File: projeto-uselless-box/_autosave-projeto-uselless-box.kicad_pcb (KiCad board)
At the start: 2 copper layers, 10 parts, among them J2 Conn_Para_Fita, M1 Motor_Servo, M2 Motor_Servo, M3 Motor_Servo, SW1 SW_DPST_x2

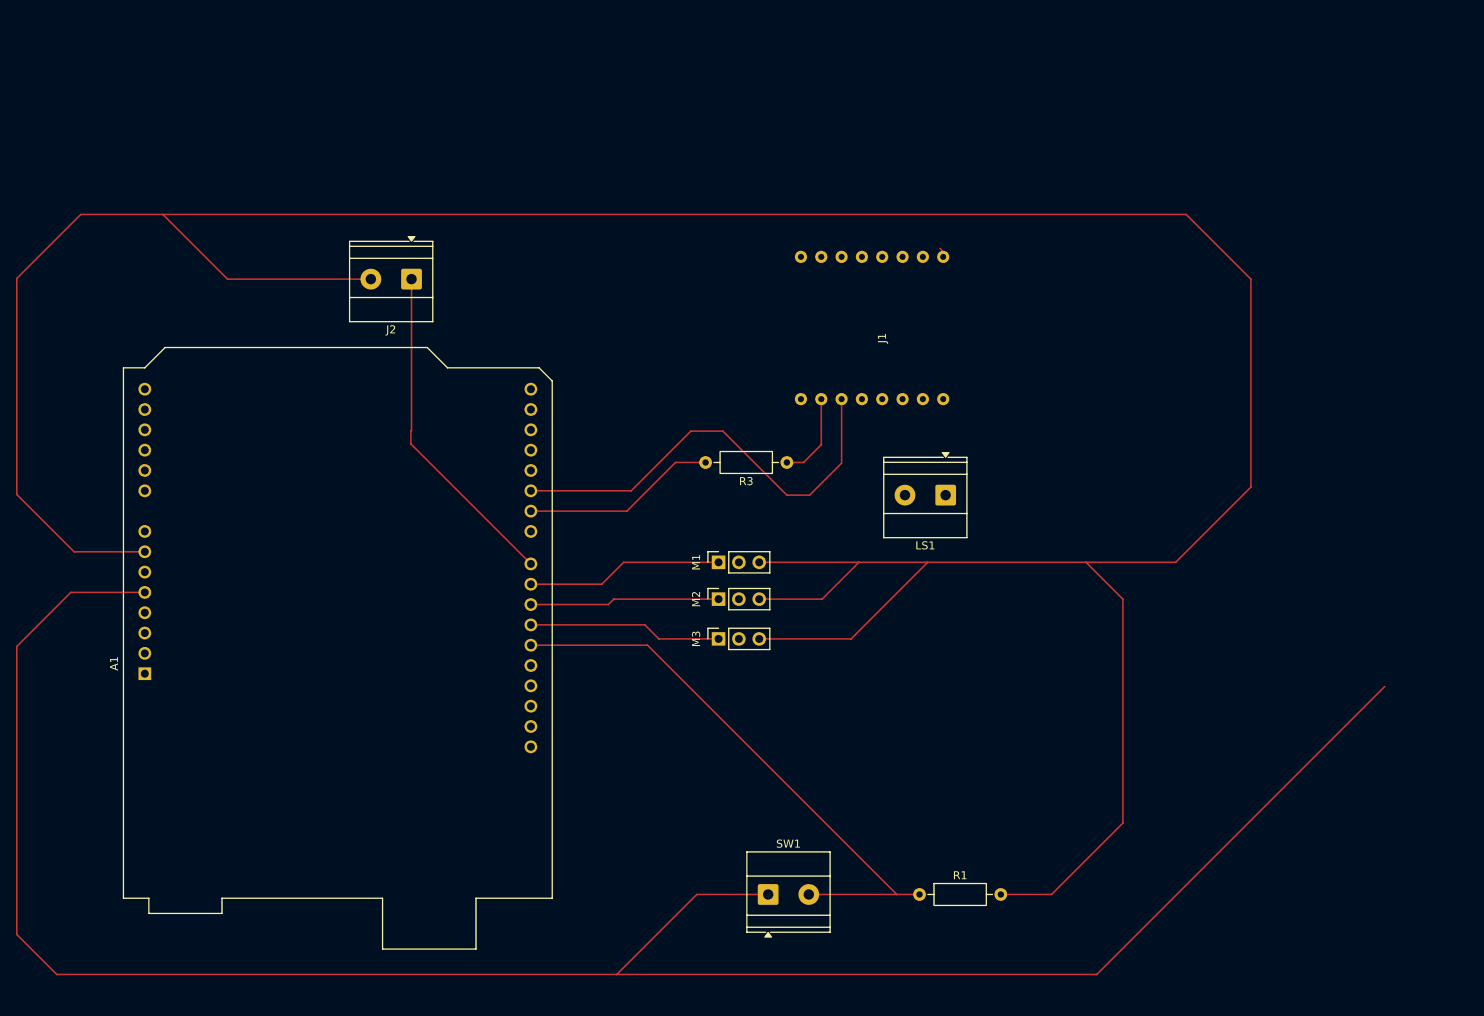
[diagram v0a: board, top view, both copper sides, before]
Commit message: Working in the Transistor of LED strip
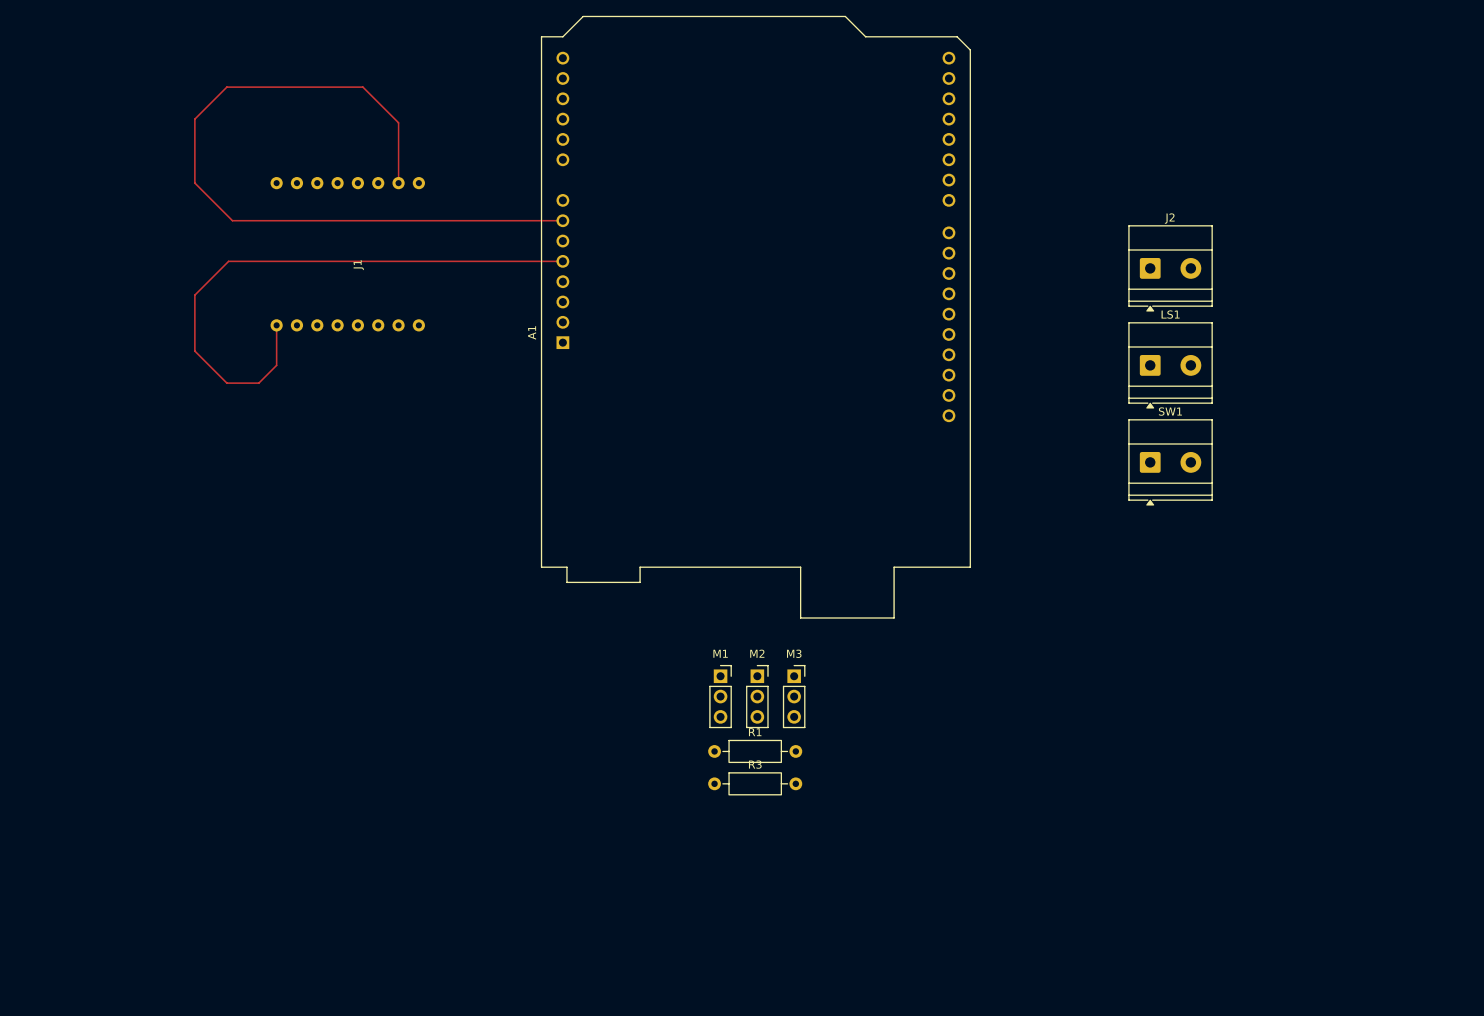
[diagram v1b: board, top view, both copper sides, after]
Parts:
- moved J2 92.3 mm to (184.4, 58.7), turned to 0 degrees
- moved SW1 72.1 mm to (184.4, 82.9)
- moved A1 66.7 mm to (111.0, 67.9)
- moved J1 66.2 mm to (75.2, 58.2)
- moved R3 41.2 mm to (130.0, 123.1), turned to 0 degrees
- moved R1 31.2 mm to (130.0, 119.0)
- moved LS1 30.3 mm to (184.4, 70.8), turned to 0 degrees
- moved M1 14.2 mm to (130.7, 109.6), turned to 0 degrees
- moved M2 10.8 mm to (135.3, 109.6), turned to 0 degrees
- moved M3 10.5 mm to (139.9, 109.6), turned to 0 degrees
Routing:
- net GND: track 420.5 -> 92.5 mm
- net +5V: track 265.8 -> 72.5 mm
- net D12: track 72.5 -> 0.00 mm
- net D5: track 54.9 -> 0.00 mm
- net D8: track 41.8 -> 0.00 mm
- net D9: track 24.6 -> 0.00 mm
- net D6: track 24.4 -> 0.00 mm
- net D11: track 24.2 -> 0.00 mm
- net D10: track 23.7 -> 0.00 mm
- net Net-(J1-RX): track 10.9 -> 0.00 mm

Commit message: Finished the first prototype of PCB
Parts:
- added J3: Conn_Para_PowerBank, TerminalBlock_Phoenix:TerminalBlock_Phoenix_MKDS-1,5-2-5.08_1x02_P5.08mm_Horizontal, F.Cu at (195.8, 73.8)
- added Q1: TIP41, Package_TO_SOT_THT:TO-220-3_Vertical, F.Cu at (181.1, 88.4)
- added R2: 100R, Resistor_THT:R_Axial_DIN0207_L6.3mm_D2.5mm_P10.16mm_Horizontal, F.Cu at (163.2, 88.4)
- M1, M2, M3: value Motor_Servo -> Motor_Servo-Edit; footprint Connector_PinSocket_2.54mm:PinSocket_1x03_P2.54mm_Vertical -> Connector_PinSocket_2.54mm:PinSocket_1x02_P2.54mm_Vertical
- moved LS1 97.4 mm to (96.0, 111.6), turned to 180 degrees
- moved M1 89.1 mm to (215.0, 80.8)
- moved M2 82.2 mm to (215.0, 89.4)
- moved M3 75.8 mm to (215.0, 99.3)
- moved R1 57.4 mm to (187.4, 118.4)
- moved R3 50.6 mm to (81.0, 110.4), turned to -90 degrees
- moved J2 40.4 mm to (195.8, 97.5), turned to -90 degrees
- moved SW1 38.9 mm to (168.5, 118.4)
- moved J1 34.5 mm to (78.2, 92.5)
- moved A1 34.5 mm to (108.7, 102.3)
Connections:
- J2 pad 1: D8 -> Net-(J2-Pin_1)
- J2 pad 2: GND -> Net-(J2-Pin_2)
- M1 pad 1: D9 -> GND
- M2 pad 1: D10 -> GND
- M3 pad 1: D11 -> GND
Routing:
- net +5V: track 72.5 -> 398.7 mm
- net GND: track 92.5 -> 318.1 mm
- net D5: track 0.00 -> 105.3 mm
- net D6: track 0.00 -> 92.0 mm
- net D12: track 0.00 -> 49.5 mm
- net Net-(J2-Pin_2): track 0.00 -> 24.6 mm
- net Net-(J2-Pin_1): track 0.00 -> 18.5 mm
- net Net-(J1-SPK2): track 0.00 -> 11.4 mm
- net Net-(J1-SPK1): track 0.00 -> 11.4 mm
- net Net-(J1-RX): track 0.00 -> 9.54 mm
- net Net-(Q1-B): track 0.00 -> 7.76 mm
- net D8: track 0.00 -> 6.29 mm
